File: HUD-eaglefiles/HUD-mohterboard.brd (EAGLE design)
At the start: 108 x 85.1 mm, 74 parts, among them U1 LM317, U2 ATMEGA328P_TQFP

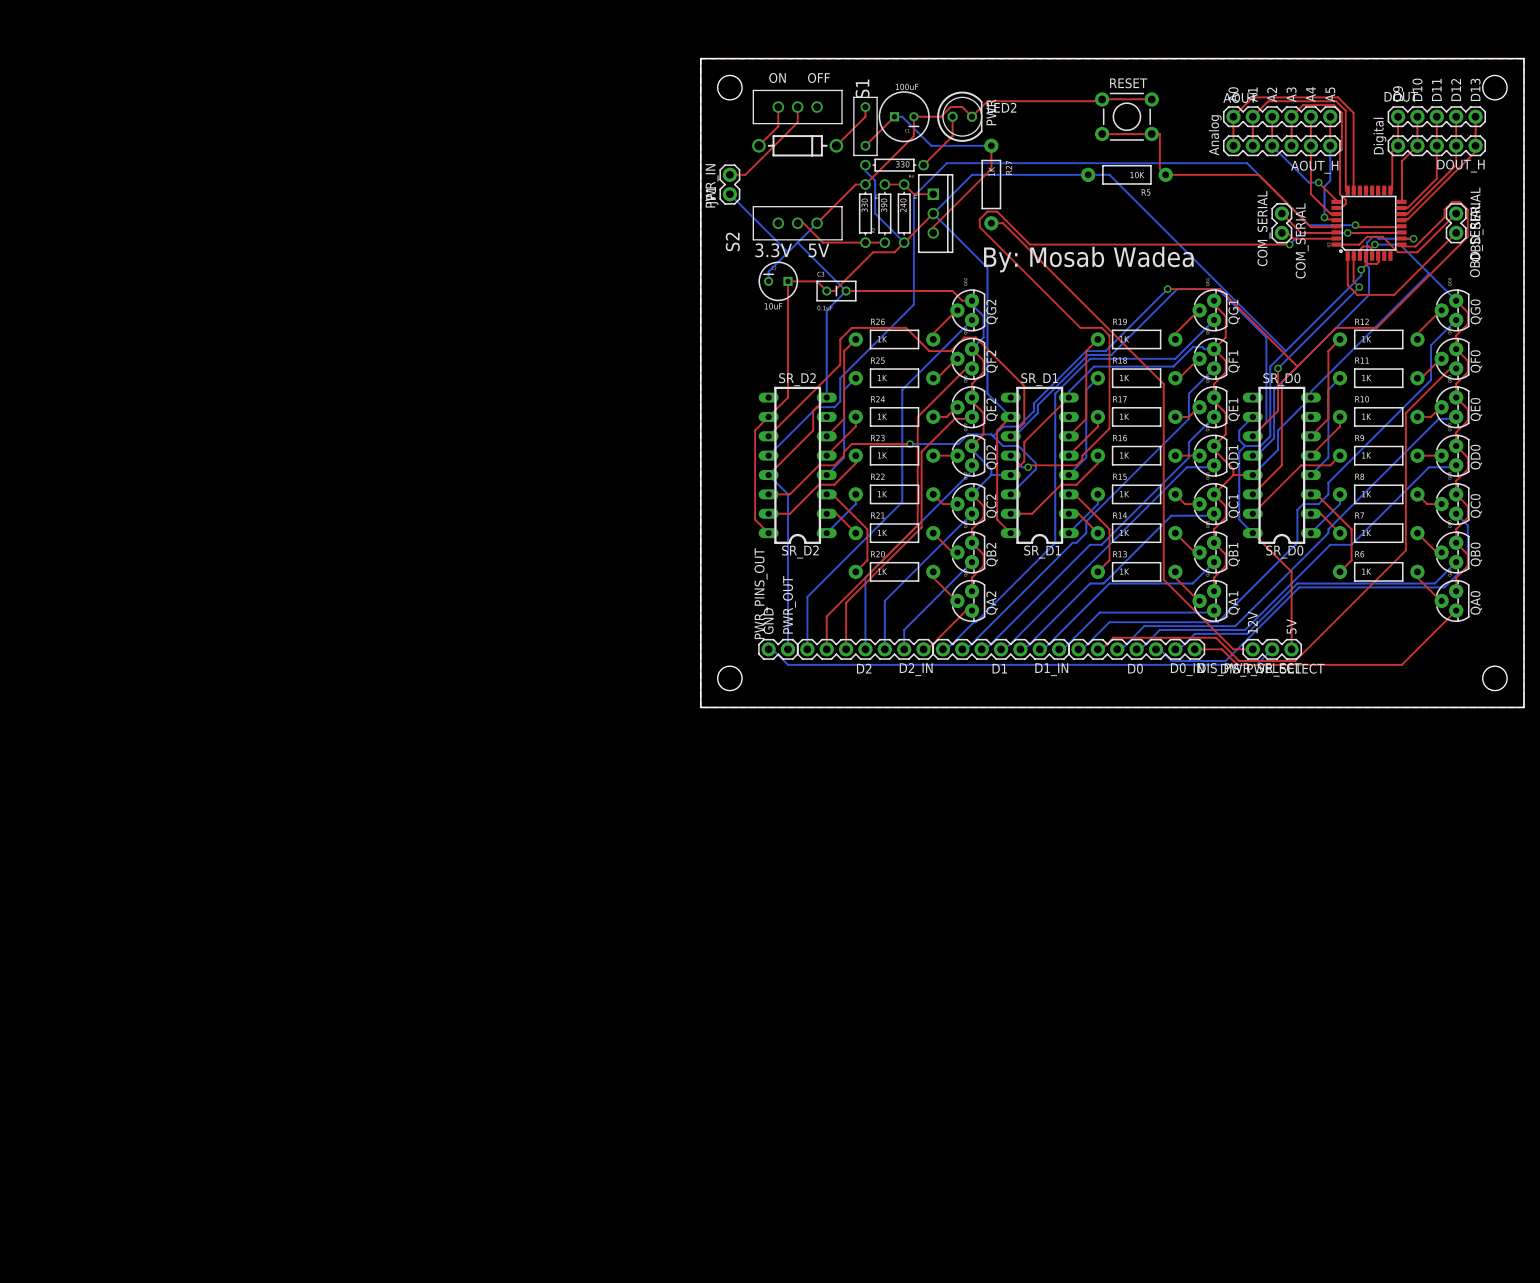
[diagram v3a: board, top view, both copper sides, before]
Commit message: changed the transistors to uln2003 (a transistor array) and rewired the schematic
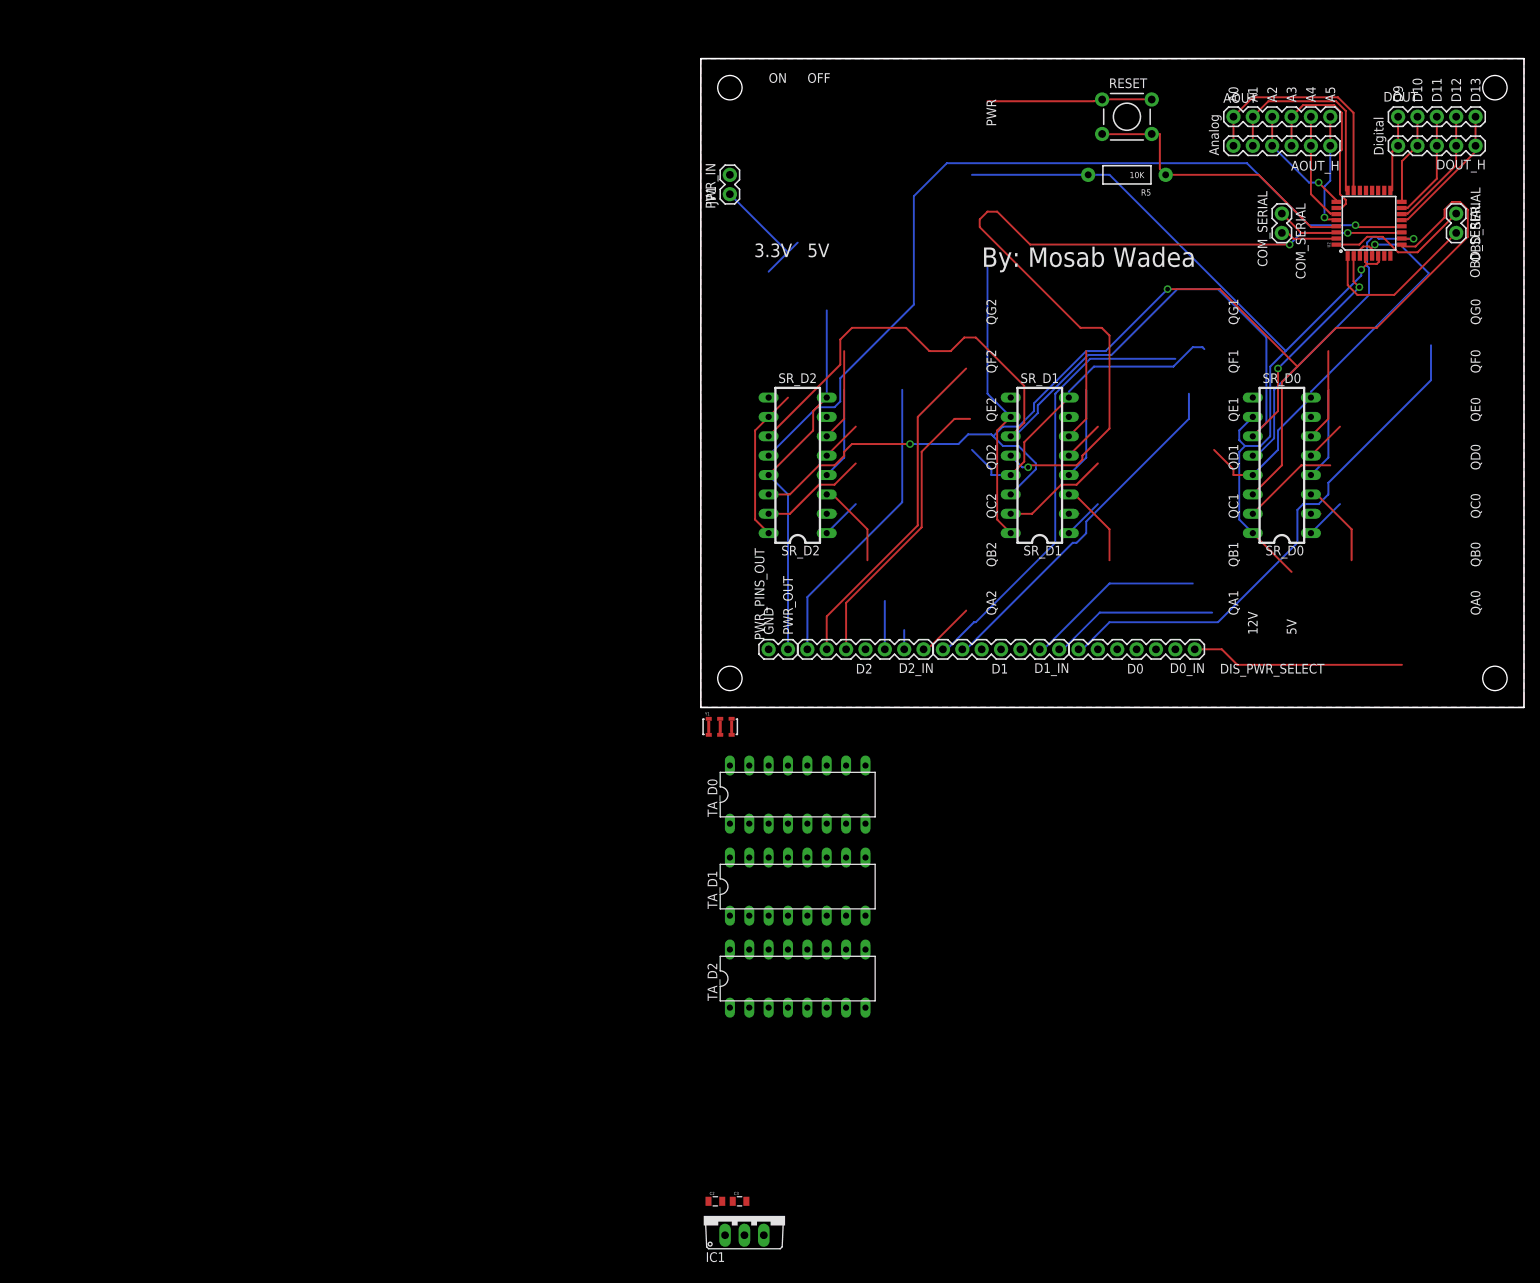
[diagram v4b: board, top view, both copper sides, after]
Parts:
- removed C1: 100uF, SparkFun:CPOL-RADIAL-100UF-25V
- removed D1: 1N4001, SparkFun:DIODE-0.4
- removed DIS_PWR_SELECT: JUMPER-3PTH, SparkFun-Retired:1X03
- removed F1: 500mA, SparkFun:PTC
- removed LED2: Power, SparkFun-Nate:LED5MM
- removed QA0, QA1, QA2, QB0, QB1, QB2, QC0, QC1, QC2, QD0, QD1, QD2, QE0, QE1, QE2, QF0, QF1, QF2, QG0, QG1, QG2: (no value), SparkFun-DiscreteSemi:TO-92
- removed R1: 240, SparkFun:AXIAL-0.3
- removed R10, R11, R12, R13, R14, R15, R16, R17, R18, R19, R20, R21, R22, R23, R24, R25, R26, R27, R6, R7, R8, R9: 1K, SparkFun-Resistors:AXIAL-0.4
- removed R2: 390, SparkFun:AXIAL-0.3
- removed R3, R4: 330, SparkFun:AXIAL-0.3
- removed S1: On/Off, SparkFun:SWITCH-SPST
- removed S2: Voltage, SparkFun:SWITCH-SPST
- removed U1: LM317, SparkFun:TO220-ADJ
- added IC1: 7805TV, linear:TO220V
- added TA_D0, TA_D1, TA_D2: ULN2003AN, uln-udn:DIL16
- added Y1: 4MHz, SparkFun-FreqCtrl:RESONATOR-SMD_MED
- C2: value 10uF -> 0.47u; device SparkFun:CPOL-RADIAL-10UF-25V -> SparkFun-Passives:0805
- C3: value 0.1uF -> 33u; device SparkFun:CAP-PTH-SMALL2 -> SparkFun-Passives:0805
- moved C2 120.9 mm to (1.91, -64.8)
- moved C3 119.9 mm to (5.08, -64.8)
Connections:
- removed net 12VOUT: DIS_PWR_SELECT.3, R27.P$2
- removed net DISPLAY_PWR-OUT: DIS_PWR_SELECT.2, PWR_PINS_OUT.1
- removed net N$20: QA1.2, R13.P$2
- removed net N$21: QC1.2, R15.P$2
- removed net N$22: QD1.2, R16.P$2
- removed net N$23: QE1.2, R17.P$2
- removed net N$24: QF1.2, R18.P$2
- removed net N$25: QB1.2, R14.P$2
- removed net N$26: QG1.2, R19.P$2
- removed net N$27: D1_IN.4, QD1.1
- removed net N$28: D1_IN.3, QC1.1
- removed net N$31: D1_IN.5, QE1.1
- removed net N$34: QC0.2, R8.P$2
- removed net N$35: QD0.2, R9.P$2
- removed net N$36: QE0.2, R10.P$2
- removed net N$37: QF0.2, R11.P$2
- removed net N$38: QB0.2, R7.P$2
- removed net N$39: QG0.2, R12.P$2
- removed net N$40: D0_IN.4, QD0.1
- removed net N$41: D0_IN.3, QC0.1
- removed net N$42: D0_IN.2, QB0.1
- removed net N$44: D0_IN.5, QE0.1
- removed net N$45: D0_IN.6, QF0.1
- removed net N$47: QA2.2, R20.P$2
- removed net N$48: QC2.2, R22.P$2
- removed net N$49: QD2.2, R23.P$2
- removed net N$50: QE2.2, R24.P$2
- removed net N$51: QF2.2, R25.P$2
- removed net N$52: QB2.2, R21.P$2
- removed net N$53: QG2.2, R26.P$2
- removed net N$54: D2_IN.4, QD2.1
- removed net PWRIN: JP1.2, S1.2
- removed net RAW: C1.1, F1.P$2, R27.P$1, U1.IN
- new net N$10: D1_IN.5, TA_D1.12
- new net N$11: D2_IN.4, TA_D2.13
- new net N$3: D0_IN.2, TA_D0.15
- new net N$7: D0_IN.6, TA_D0.11
- new net N$9: D1_IN.4, TA_D1.13
- new net VS: C2.1, IC1.1, JP1.2, PWR_PINS_OUT.1
- net A0: now also TA_D0.1; no longer R6.P$1
- net A1: now also TA_D1.1; no longer R13.P$1
- net A2: now also TA_D2.1; no longer R20.P$1
- net B0: now also TA_D0.2; no longer R7.P$1
- net B1: now also TA_D1.2; no longer R14.P$1
- net B2: now also TA_D2.2; no longer R21.P$1
- net C0: now also TA_D0.3; no longer R8.P$1
- net C1: now also TA_D1.3; no longer R15.P$1
- net C2: now also TA_D2.3; no longer R22.P$1
- net D0: now also TA_D0.4; no longer R9.P$1
- net D1: now also TA_D1.4; no longer R16.P$1
- net D2: now also TA_D2.4; no longer R23.P$1
- net E0: now also TA_D0.5; no longer R10.P$1
- net E1: now also TA_D1.5; no longer R17.P$1
- net E2: now also TA_D2.5; no longer R24.P$1
- net F0: now also TA_D0.6; no longer R11.P$1
- net F1: now also TA_D1.6; no longer R18.P$1
- net F2: now also TA_D2.6; no longer R25.P$1
- net G0: now also TA_D0.7; no longer R12.P$1
- net G1: now also TA_D1.7; no longer R19.P$1
- net G2: now also TA_D2.7; no longer R26.P$1
- net GND: now also IC1.2, TA_D0.8, TA_D1.8, TA_D2.8, Y1.2; no longer C1.2, LED2.K, QA0.3, QA1.3, QA2.3, QB0.3, QB1.3, QB2.3, QC0.3, QC1.3, QC2.3, QD0.3, QD1.3, QD2.3, QE0.3, QE1.3, QE2.3, QF0.3, QF1.3, QF2.3, QG0.3, QG1.3, QG2.3, R3.P$1, S2.3
- net N$1: now also U2.7, Y1.1; no longer D1.C, F1.P$1
- net N$2: now also U2.8, Y1.3; no longer D1.A, S1.3
- net N$29: now also TA_D1.15; no longer QB1.1
- net N$30: now also TA_D1.16; no longer QA1.1
- net N$32: now also TA_D1.11; no longer QF1.1
- net N$33: now also TA_D1.10; no longer QG1.1
- net N$4: now also D0_IN.3, TA_D0.14; no longer R2.P$1, R3.P$2, S2.2
- net N$43: now also TA_D0.16; no longer QA0.1
- net N$46: now also TA_D0.10; no longer QG0.1
- net N$5: now also D0_IN.4, TA_D0.13; no longer R1.P$1, R2.P$2, U1.ADJ
- net N$55: now also TA_D2.14; no longer QC2.1
- net N$56: now also TA_D2.15; no longer QB2.1
- net N$57: now also TA_D2.16; no longer QA2.1
- net N$58: now also TA_D2.12; no longer QE2.1
- net N$59: now also TA_D2.11; no longer QF2.1
- net N$6: now also D0_IN.5, TA_D0.12; no longer QA0.2, R6.P$2
- net N$60: now also TA_D2.10; no longer QG2.1
- net N$8: now also D1_IN.3, TA_D1.14; no longer LED2.A, R4.P$1
- net VCC: now also IC1.3; no longer C2.1, DIS_PWR_SELECT.1, R1.P$2, R4.P$2, U1.OUT
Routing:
- net GND: track 389.2 -> 186.9 mm
- net VCC: track 247.2 -> 168.5 mm
- net N$45: track 75.3 -> 0.00 mm
- net 12VOUT: track 72.5 -> 0.00 mm
- net DISPLAY_PWR-OUT: track 67.7 -> 0.00 mm
- net N$44: track 57.4 -> 0.00 mm
- net N$41: track 54.2 -> 0.00 mm
- net N$40: track 51.9 -> 0.00 mm
- net N$31: track 44.3 -> 0.00 mm
- net N$42: track 41.6 -> 0.00 mm
- net N$27: track 37.9 -> 0.00 mm
- net RAW: track 34.3 -> 0.00 mm
- net N$28: track 32.8 -> 0.00 mm
- net N$54: track 29.9 -> 0.00 mm
- net N$55: track 22.5 -> 6.35 mm
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
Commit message: new layout for the new schematic
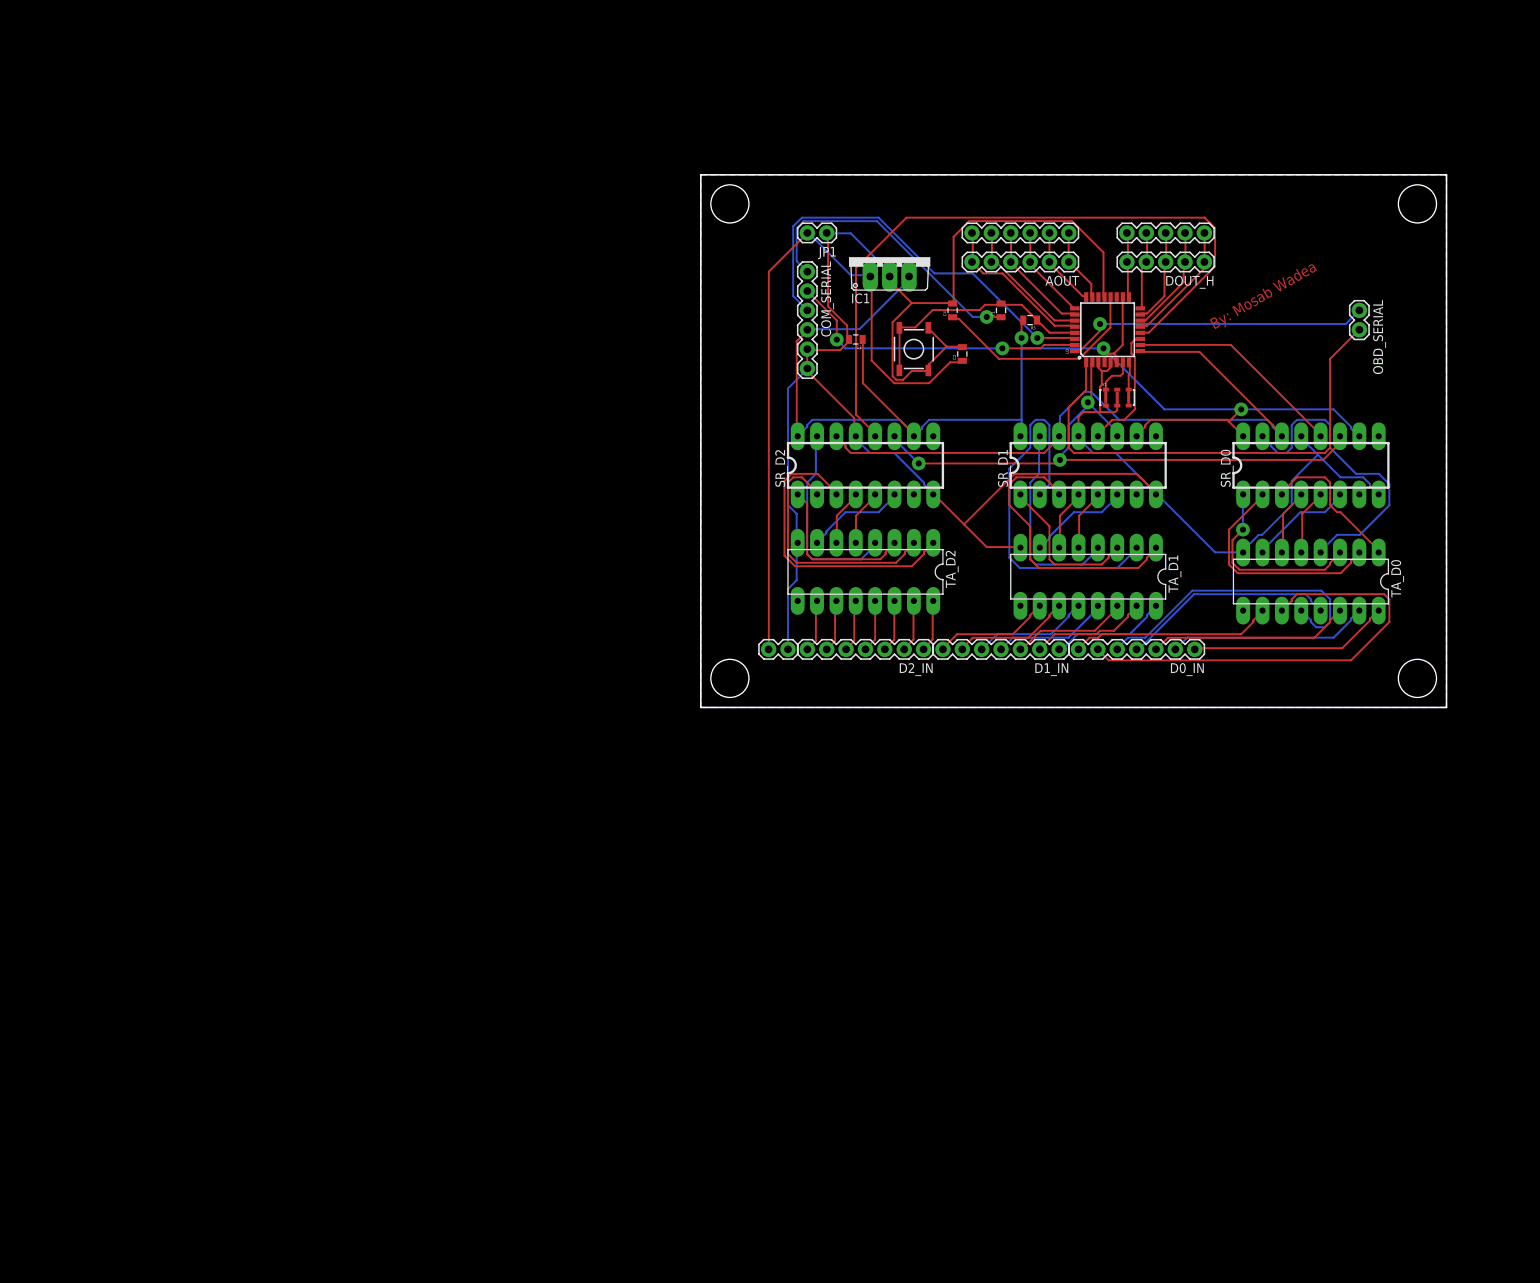
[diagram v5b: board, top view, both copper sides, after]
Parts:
- added C1, C4: 0.1uF, SparkFun-Passives:0805
- COM_SERIAL: device SparkFun-Connectors:1X02 -> SparkFun-Connectors:1X06
- R5: device SparkFun-Resistors:AXIAL-0.4 -> SparkFun-Resistors:0805
- RESET: value TS42031-160R-TR-7260 -> TAC_SWITCHSMD; device SparkFun-Retired:TACTILE-PTH -> SparkFun-Retired:TACTILE-SWITCH-SMD
- moved IC1 127.2 mm to (24.8, 59.1)
- moved C2 115.7 mm to (34.3, 46.4), turned to 90 degrees
- moved C3 114.1 mm to (20.3, 48.3), turned to 180 degrees
- moved TA_D0 72.9 mm to (80.0, 16.5), turned to 180 degrees
- moved Y1 67.6 mm to (54.6, 40.6)
- moved COM_SERIAL 62.7 mm to (14.0, 57.1)
- moved TA_D1 55.7 mm to (50.8, 17.1), turned to 180 degrees
- moved TA_D2 54.1 mm to (21.6, 17.8), turned to 180 degrees
- moved RESET 41.3 mm to (27.9, 47.0), turned to 270 degrees
- moved DOUT 38.7 mm to (66.0, 62.2)
- moved DOUT_H 38.7 mm to (66.0, 58.4)
- moved U2 37.0 mm to (53.3, 49.5)
- moved AOUT 28.8 mm to (48.3, 58.4), turned to 180 degrees
- moved AOUT_H 24.4 mm to (48.3, 62.2), turned to 180 degrees
- moved R5 22.9 mm to (43.2, 50.8)
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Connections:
- new net DTR: C1.1, COM_SERIAL.1
- new net N$12: C4.1, U2.20
- net GND: now also C4.2, COM_SERIAL.5, COM_SERIAL.6, U2.21
- net RESET_WIRE: now also C1.2, R5.1; no longer R5.P$1
- net RX: now also COM_SERIAL.3; no longer COM_SERIAL.1
- net VCC: now also COM_SERIAL.4, R5.2, U2.18; no longer R5.P$2
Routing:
- net GND: track 186.9 -> 293.5 mm, vias 1 -> 0
- net CE_D1: track 110.3 -> 17.0 mm, vias 3 -> 0
- net VS: track 0.00 -> 93.0 mm
- net SR_SDATA: track 162.8 -> 90.5 mm, vias 2 -> 0
- net N$7: track 0.00 -> 59.3 mm
- net SR_CLK: track 141.5 -> 82.6 mm, vias 2 -> 3
- net B1: track 1.27 -> 49.6 mm
- net RX: track 8.24 -> 55.8 mm, vias 0 -> 1
- net N$33: track 57.7 -> 15.3 mm
- net N$46: track 68.8 -> 26.4 mm
- net OBD_TX: track 22.0 -> 64.0 mm
- net N$6: track 0.00 -> 39.7 mm
- net DTR: track 0.00 -> 38.7 mm, vias 0 -> 1
- net N$59: track 44.4 -> 6.96 mm
- net TX: track 7.47 -> 39.9 mm, vias 0 -> 2
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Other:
- board size 108 x 85.1 mm -> 97.8 x 69.8 mm
- board text removed: "12V"
- board text removed: "3.3V"
- board text removed: "5V"
- board text removed: "A0"
- board text removed: "A1"
- board text removed: "A2"
- board text removed: "A3"
- board text removed: "A4"
- board text removed: "A5"
- board text removed: "Analog"
- board text removed: "COM_SERIAL"
- board text removed: "D0"
- board text removed: "D1"
- board text removed: "D10"
- board text removed: "D11"
- board text removed: "D12"
- board text removed: "D13"
- board text removed: "D2"
- board text removed: "D9"
- board text removed: "DIS_PWR_SELECT"
- board text removed: "Digital"
- board text removed: "GND"
- board text removed: "OBD_SERIAL"
- board text removed: "OFF"
- board text removed: "ON"
- board text removed: "PWR"
- board text removed: "PWR_IN"
- board text removed: "PWR_OUT"
- board text removed: "QA0"
- board text removed: "QA1"
- board text removed: "QA2"
- board text removed: "QB0"
- board text removed: "QB1"
- board text removed: "QB2"
- board text removed: "QC0"
- board text removed: "QC1"
- board text removed: "QC2"
- board text removed: "QD0"
- board text removed: "QD1"
- board text removed: "QD2"
- board text removed: "QE0"
- board text removed: "QE1"
- board text removed: "QE2"
- board text removed: "QF0"
- board text removed: "QF1"
- board text removed: "QF2"
- board text removed: "QG0"
- board text removed: "QG1"
- board text removed: "QG2"
- board text removed: "SR_D0"
- board text removed: "SR_D1"
- board text removed: "SR_D2"
